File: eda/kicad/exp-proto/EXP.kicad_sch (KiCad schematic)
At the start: 23 parts, among them J1 IN, J2 IN, J3 OUT, J4 OUT, J5 On, J6 On, J7 KEYPAD, J8 INTR, U1 74F138, U2 74F138, U3 74F574, U4 74F174, U5 74F244, U6 MCP1702-5002E

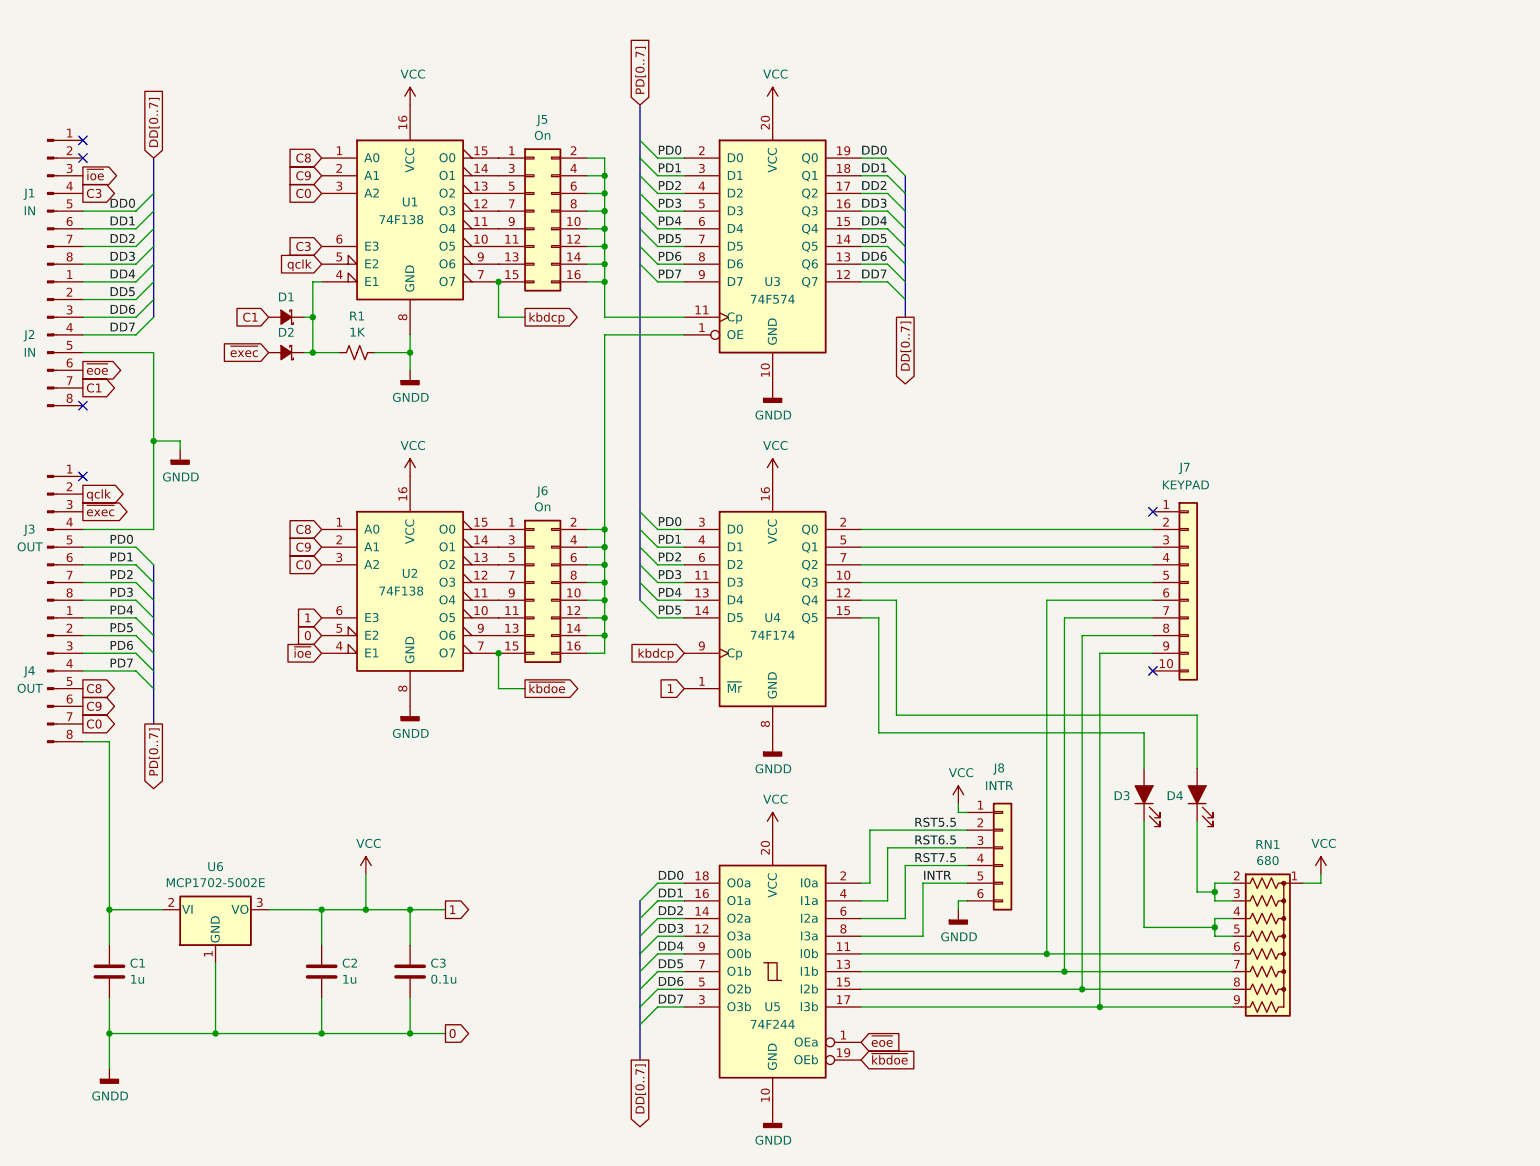
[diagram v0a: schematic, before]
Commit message: add notes to schematic
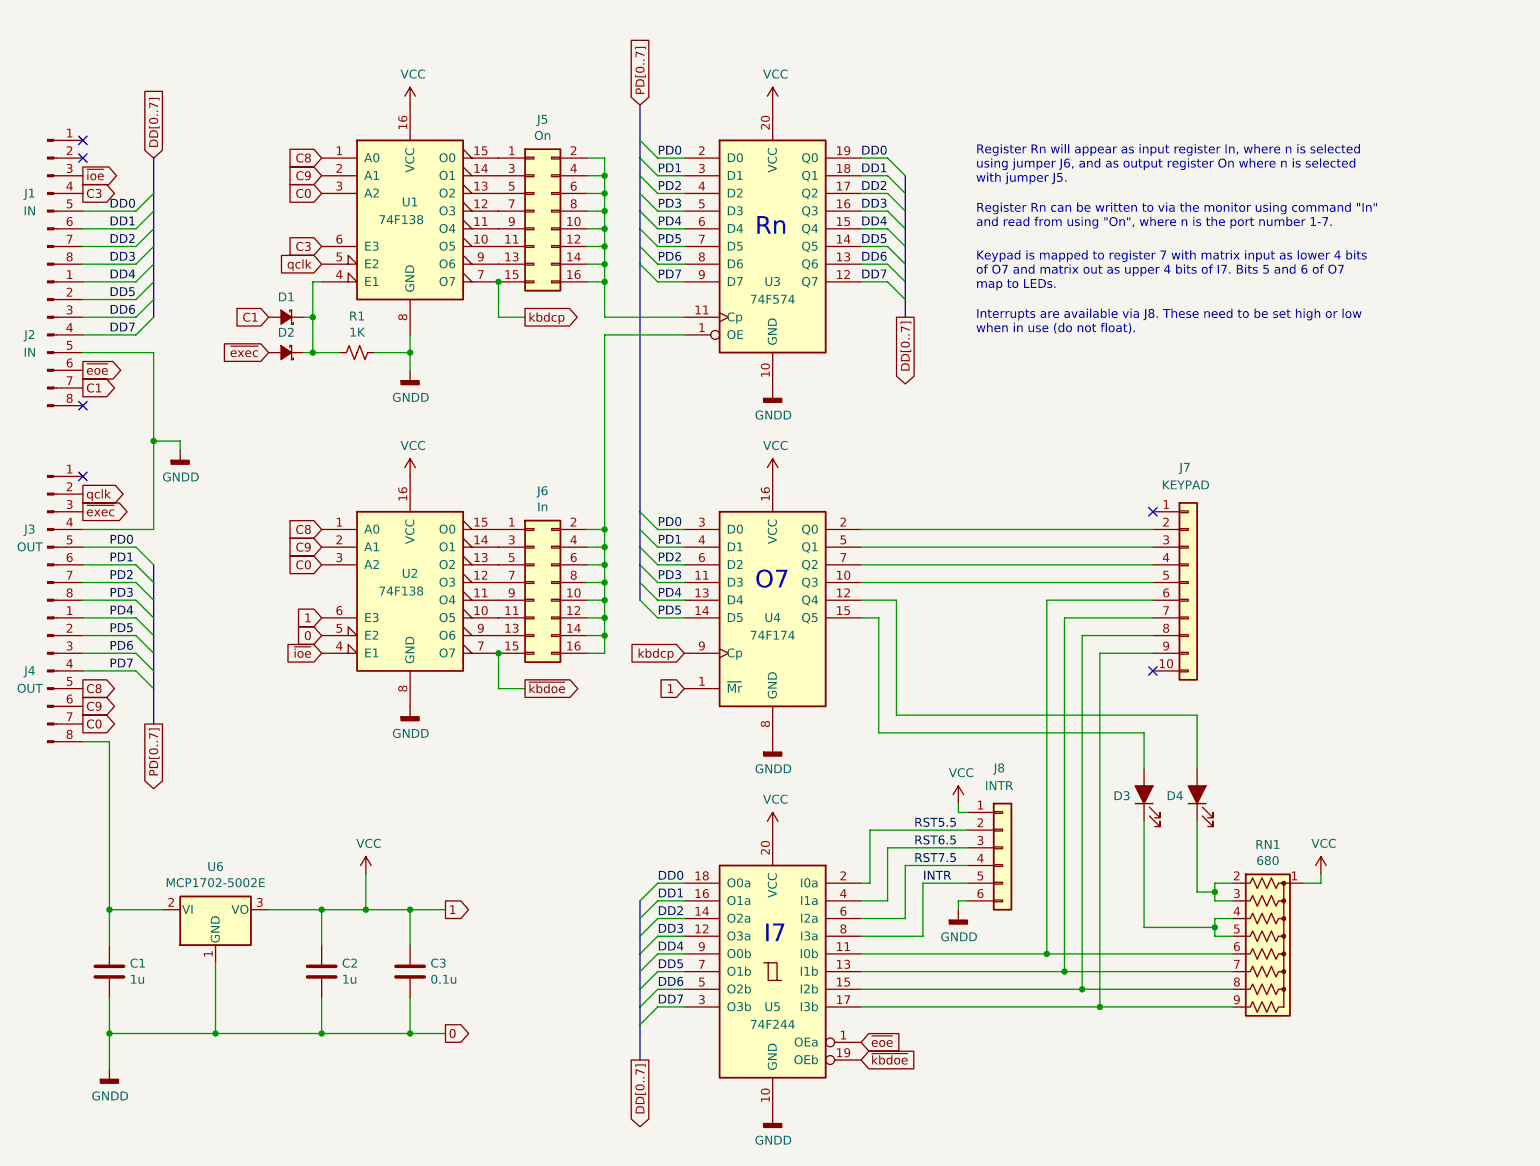
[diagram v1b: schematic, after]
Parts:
- J6: value On -> In
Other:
- note added: "I7"
- note added: "Interrupts are available via J8. These need to be set high or low when in use (do not float)."
- note added: "Keypad is mapped to register 7 with matrix input as lower 4 bits of O7 and matrix out as upper 4 bits of I7. Bits 5 and 6 of O7 map to LEDs."
- note added: "O7"
- note added: "Register Rn can be written to via the monitor using command "In" and read from using "On", where n is the port number 1-7."
- note added: "Register Rn will appear as input register In, where n is selected using jumper J6, and as output register On where n is selected with jumper J5."
- note added: "Rn"
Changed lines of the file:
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@@
     (stroke (width 0) (type default) (color 0 0 0 0))
+  )
+  (text "Register Rn can be written to via the monitor using command \"In\" \nand read from using \"On\", where n is the port number 1-7."
+    (at 160.02 45.72 0)
+    (effects (font (size 1.27 1.27)) (justify left bottom))
+  )
+  (text "I7" (at 129.54 148.59 0)
+    (effects (font (size 2.54 2.54)) (justify left bottom))
+  )
+  (text "Interrupts are available via J8. These need to be set high or low\nwhen in use (do not float)."
+    (at 160.02 60.96 0)
+    (effects (font (size 1.27 1.27)) (justify left bottom))
+  )
+  (text "Keypad is mapped to register 7 with matrix input as lower 4 bits\nof O7 and matrix out as upper 4 bits of I7. Bits 5 and 6 of O7\nmap to LEDs."
+    (at 160.02 54.61 0)
+    (effects (font (size 1.27 1.27)) (justify left bottom))
+  )
+  (text "Register Rn will appear as input register In, where n is selected \nusing jumper J6, and as output register On where n is selected \nwith jumper J5."
+    (at 160.02 39.37 0)
+    (effects (font (size 1.27 1.27)) (justify left bottom))
+  )
+  (text "O7" (at 128.27 97.79 0)
+    (effects (font (size 2.54 2.54)) (justify left bottom))
+  )
+  (text "Rn" (at 128.27 46.99 0)
+    (effects (font (size 2.54 2.54)) (justify left bottom))
   )
   (label "PD5" (at 114.3 101.6 0)
@@
     (in_bom yes) (on_board yes)
     (property "Reference" "J6" (id 0) (at 97.79 83.3882 0))
-    (property "Value" "On" (id 1) (at 97.79 85.6996 0))
+    (property "Value" "In" (id 1) (at 97.79 85.6996 0))
     (property "Footprint" "Connector_PinHeader_2.54mm:PinHeader_2x08_P2.54mm_Vertical" (id 2) (at 96.52 96.52 0)
       (effects (font (size 1.27 1.27)) hide)
@@
     )
     (path "/00000000-0000-0000-0000-00005f5d794d"
-      (reference "J6") (unit 1) (value "On") (footprint "Connector_PinHeader_2.54mm:PinHeader_2x08_P2.54mm_Vertical")
+      (reference "J6") (unit 1) (value "In") (footprint "Connector_PinHeader_2.54mm:PinHeader_2x08_P2.54mm_Vertical")
     )
     (path "/00000000-0000-0000-0000-00005de27ae4"
